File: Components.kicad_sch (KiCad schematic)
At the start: 29 parts, among them SW25 SW_PUSH, SW36 SW_PUSH, SW40 SW_PUSH, U1 SRV05-4, X1 Crystal_GND24_Small

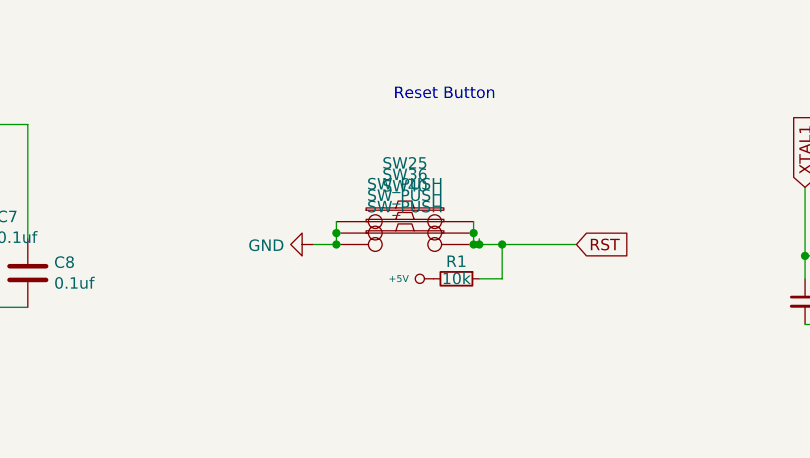
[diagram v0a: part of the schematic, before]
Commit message: edited schematics, assigned footprints
4u spacebar missing, no appropriate footprint in library yet
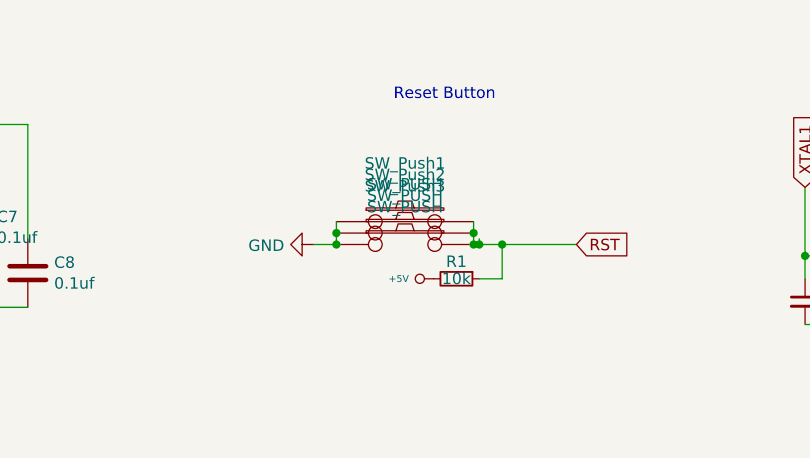
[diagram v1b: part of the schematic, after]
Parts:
- renumbered SW25 to SW_Push1, SW36 to SW_Push2, SW40 to SW_Push3
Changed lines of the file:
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@@
   (symbol (lib_id "keyboard_parts:SW_PUSH") (at 200.025 36.83 0) (unit 1)
     (in_bom yes) (on_board yes)
-    (property "Reference" "SW25" (id 0) (at 200.025 30.353 0))
+    (property "Reference" "SW_Push1" (id 0) (at 200.025 30.353 0))
     (property "Value" "SW_PUSH" (id 1) (at 200.025 32.6644 0))
     (property "Footprint" "Button_Switch_SMD:SW_SPST_SKQG_WithoutStem" (id 2) (at 200.025 36.83 0)
@@
   (symbol (lib_id "keyboard_parts:SW_PUSH") (at 200.025 38.1 0) (unit 1)
     (in_bom yes) (on_board yes)
-    (property "Reference" "SW36" (id 0) (at 200.025 31.623 0))
+    (property "Reference" "SW_Push2" (id 0) (at 200.025 31.623 0))
     (property "Value" "SW_PUSH" (id 1) (at 200.025 33.9344 0))
     (property "Footprint" "Connector_PinHeader_2.54mm:PinHeader_1x02_P2.54mm_Vertical" (id 2) (at 200.025 38.1 0)
@@
   (symbol (lib_id "keyboard_parts:SW_PUSH") (at 200.025 39.37 0) (unit 1)
     (in_bom yes) (on_board yes)
-    (property "Reference" "SW40" (id 0) (at 200.025 32.893 0))
+    (property "Reference" "SW_Push3" (id 0) (at 200.025 32.893 0))
     (property "Value" "SW_PUSH" (id 1) (at 200.025 35.2044 0))
     (property "Footprint" "Button_Switch_SMD:SW_SPST_SKQG_WithoutStem" (id 2) (at 200.025 39.37 0)
